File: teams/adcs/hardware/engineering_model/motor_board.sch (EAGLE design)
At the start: 63 parts

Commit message: ADCS/RW: Utilize design block in further routing progress
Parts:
- removed BRKMOD_X, BRKMOD_Y, BRKMOD_Z, CMTMOD_Y: 0_OHM_JUMPER, DubSat1 Components:0_OHM_JUMPER
- removed C16: 2.2uF, rcl:C-USC1206
- removed C17, C19: 0.1uF, rcl:C-USC0805
- removed C18, C20: 1uF, rcl:C-USC1206
- removed R25, R26, R27, R32: 3.3K, rcl:R-US_R0805
- removed R28, R29, R30: 10K, rcl:R-US_R0805
- removed R31: (no value), rcl:R-US_R0805
- removed U$12: DRV10970, DubSat1 Components:DRV10970
- added C1: 2.2uF, rcl:C-USC1206
- added C2, C4: 0.1uF, rcl:C-USC0805
- added C3, C5: 1uF, rcl:C-USC1206
- added CMTMODY: 0_OHM_JUMPER, DubSat1 Components:0_OHM_JUMPER
- added R1, R2, R3, R8: 3.3K, rcl:R-US_R0805
- added R4, R5, R6: 10K, rcl:R-US_R0805
- added R7: (no value), rcl:R-US_R0805
- added SERIAL_Z, SERIAL_Z1, SERIAL_Z2: (no value), SparkFun-Connectors:CONN_03LOCK
- added U$13: DRV10970, DubSat1 Components:DRV10970
- R12: value 3.3K -> 10K
- R15: value 10K -> (none)
- R16: value (none) -> 3.3K
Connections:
- net N$20 renamed RETRY_Z
- net N$24 renamed VCP_Z
- net N$50 renamed CPP_Z
- net N$51 renamed CPN_Z
- removed net N$13: C11.1, U$7.RETRY
- removed net N$14: C13.2, U$7.VCP
- removed net N$15: R18.2, R19.1, U$7.U_HN, U$7.V_HN, U$7.W_HN
- removed net N$16: DAA_Y.SIG, U$7.DAA
- removed net N$17: CMTMOD_Y.SIG, U$7.CMTMOD
- removed net N$18: BRKMOD_Y.SIG, U$7.BRKMOD
- removed net N$21: C12.2, U$7.CPP
- removed net N$22: C12.1, U$7.CPN
- removed net N$23: MOTOR_Y.P$1, U$7.W
- removed net N$25: MOTOR_Y.P$2, U$7.V
- removed net N$30: R11.2, R12.1, U$10.U_HN, U$10.V_HN, U$10.W_HN
- removed net N$36: DAA_X.SIG, U$10.DAA
- removed net N$38: CMTMOD_X.SIG, U$10.CMTMOD
- removed net N$39: BRKMOD_X.SIG, U$10.BRKMOD
- removed net N$40: MOTOR_Y.P$6, R22.2, U$7.W_HP
- removed net N$41: MOTOR_Y.P$7, R21.2, U$7.V_HP
- removed net N$52: MOTOR_X.P$1, U$10.W
- removed net N$53: MOTOR_X.P$2, U$10.V
- removed net N$54: MOTOR_X.P$6, R15.2, U$10.W_HP
- removed net N$55: MOTOR_X.P$7, R14.2, U$10.V_HP
- removed net N$57: MOTOR_X.P$8, R13.2, U$10.U_HP
- removed net N$58: R16.2, U$10.CS
- removed net N$59: MOTOR_X.P$3, U$10.U
- removed net N$60: MOTOR_Y.P$8, R20.2, U$7.U_HP
- removed net N$61: R23.2, U$7.CS
- removed net N$62: MOTOR_Y.P$3, U$7.U
- removed net N$69: C16.1, U$12.RETRY
- removed net N$70: C18.2, U$12.VCP
- removed net N$71: R26.2, R27.1, U$12.U_HN, U$12.V_HN, U$12.W_HN
- removed net N$72: DAA_Z.SIG, U$12.DAA
- removed net N$73: CMTMOD_Z.SIG, U$12.CMTMOD
- removed net N$74: BRKMOD_Z.SIG, U$12.BRKMOD
- removed net N$75: C17.2, U$12.CPP
- removed net N$76: C17.1, U$12.CPN
- removed net N$77: MOTOR_Z.P$1, U$12.W
- removed net N$78: MOTOR_Z.P$2, U$12.V
- removed net N$79: MOTOR_Z.P$6, R30.2, U$12.W_HP
- removed net N$80: MOTOR_Z.P$7, R29.2, U$12.V_HP
- removed net N$81: MOTOR_Z.P$8, R28.2, U$12.U_HP
- removed net N$82: R31.2, U$12.CS
- removed net N$83: MOTOR_Z.P$3, U$12.U
- removed net VM_X: C10.2, U$10.VM
- removed net VM_Y: C15.2, U$7.VM
- new net BRKMOD_X: U$7.BRKMOD
- new net BRKMOD_Y: U$13.BRKMOD
- new net BRKMOD_Z: U$10.BRKMOD
- new net CMTMOD_X: CMTMOD_X.SIG, U$7.CMTMOD
- new net CMTMOD_Y: CMTMODY.SIG, U$13.CMTMOD
- new net CMTMOD_Z: CMTMOD_Z.SIG, U$10.CMTMOD
- new net CPN_X: C2.1, U$7.CPN
- new net CPN_Y: C12.1, U$13.CPN
- new net CPP_X: C2.2, U$7.CPP
- new net CPP_Y: C12.2, U$13.CPP
- new net CS_X: R7.2, U$7.CS
- new net CS_Y: R23.2, U$13.CS
- new net CS_Z: R15.2, U$10.CS
- new net DAA_X: DAA_X.SIG, U$7.DAA
- new net DAA_Y: DAA_Y.SIG, U$13.DAA
- new net DAA_Z: DAA_Z.SIG, U$10.DAA
- new net FG: U$8.P7.4_GPIO
- new net FR: U$8.P7.3_GPIO
- new net HN_X: R2.2, R3.1, U$7.U_HN, U$7.V_HN, U$7.W_HN
- new net HN_Y: R18.2, R19.1, U$13.U_HN, U$13.V_HN, U$13.W_HN
- new net HN_Z: R10.2, R11.1, U$10.U_HN, U$10.V_HN, U$10.W_HN
- new net HP_U_X: MOTOR_X.P$8, R4.2, U$7.U_HP
- new net HP_U_Y: MOTOR_Y.P$8, R20.2, U$13.U_HP
- new net HP_U_Z: MOTOR_Z.P$8, R12.2, U$10.U_HP
- new net HP_V_X: MOTOR_X.P$7, R5.2, U$7.V_HP
- new net HP_V_Y: MOTOR_Y.P$7, R21.2, U$13.V_HP
- new net HP_V_Z: MOTOR_Z.P$7, R13.2, U$10.V_HP
- new net HP_W_X: MOTOR_X.P$6, R6.2, U$7.W_HP
- new net HP_W_Y: MOTOR_Y.P$6, R22.2, U$13.W_HP
- new net HP_W_Z: MOTOR_Z.P$6, R14.2, U$10.W_HP
- new net M_Z_RX: SERIAL_Z.2, SERIAL_Z1.2, SERIAL_Z2.2, U$8.P2.6_GPIO/PWM
- new net M_Z_TX: SERIAL_Z.1, SERIAL_Z1.1, SERIAL_Z2.1, U$8.P2.5_GPIO
- new net PWM: U$8.P1.7_GPIO/PWM
- new net RD: U$8.P4.0_GPIO
- new net RETRY_X: C1.1, U$7.RETRY
- new net RETRY_Z_Y: C11.1, U$13.RETRY
- new net U_X: MOTOR_X.P$3, U$7.U
- new net U_Y: MOTOR_Y.P$3, U$13.U
- new net U_Z: MOTOR_Z.P$3, U$10.U
- new net V1_Z: MOTOR_Z.P$2, U$10.V
- new net VCP_X: C3.2, U$7.VCP
- new net VCP_Y: C13.2, U$13.VCP
- new net VM: C15.2, C5.2, U$13.VM, U$7.VM
- new net V_X: MOTOR_X.P$2, U$7.V
- new net V_Y: MOTOR_Y.P$2, U$13.V
- new net W_X: MOTOR_X.P$1, U$7.W
- new net W_Y: MOTOR_Y.P$1, U$13.W
- new net W_Z: MOTOR_Z.P$1, U$10.W
- net FG_X: now also R8.2, U$7.FG; no longer R17.2, U$10.FG
- net FG_Y: now also U$13.FG; no longer U$7.FG
- net FG_Z: now also R16.2, U$10.FG; no longer R32.2, U$12.FG, U$8.P7.4_GPIO
- net FR_X: now also U$7.FR; no longer U$10.FR
- net FR_Y: now also U$13.FR; no longer U$7.FR
- net FR_Z: now also U$10.FR; no longer U$12.FR, U$8.P7.3_GPIO
- net GND: now also C1.2, C3.1, C4.1, C5.1, CMTMODY.GND, R10.1, R15.1, R2.1, R7.1, SERIAL_Z.3, SERIAL_Z1.3, SERIAL_Z2.3, U$13.GND; no longer BRKMOD_X.GND, BRKMOD_Y.GND, BRKMOD_Z.GND, C16.2, C18.1, C19.1, C20.1, CMTMOD_Y.GND, R11.1, R16.1, R26.1, R31.1, U$12.GND
- net PWM_X: now also U$7.PWM; no longer U$10.PWM
- net PWM_Y: now also U$13.PWM; no longer U$7.PWM
- net PWM_Z: now also U$10.PWM; no longer U$12.PWM, U$8.P1.7_GPIO/PWM
- net RD_X: now also R1.1, U$7.RD; no longer R9.1, U$10.RD
- net RD_Y: now also R17.1, U$13.RD; no longer R10.1, U$7.RD
- net RD_Z: now also R9.1, U$10.RD; no longer R25.1, U$12.RD, U$8.P4.0_GPIO
- net VINT_X: now also C4.2, R1.2, R3.2, R4.1, R5.1, R6.1, R8.1, U$7.VINT; no longer BRKMOD_X.VCC, C9.2, R12.2, R13.1, R14.1, R15.1, R17.1, R9.2, U$10.VINT
- net VINT_Y: now also CMTMODY.VCC, R17.2, U$13.VINT; no longer BRKMOD_Y.VCC, CMTMOD_Y.VCC, R10.2, U$7.VINT
- net VINT_Z: now also C9.2, R11.2, R12.1, R13.1, R14.1, R16.1, R9.2, U$10.VINT; no longer BRKMOD_Z.VCC, C19.2, R25.2, R27.2, R28.1, R29.1, R30.1, R32.1, U$12.VINT
- net VM_Z: now also C10.2, U$10.VM; no longer C20.2, U$12.VM
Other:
- moved on the sheet: C10, C11, C12, C13, C14, C15, C6, C7, C8, C9, CMTMOD_X, CMTMOD_Z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

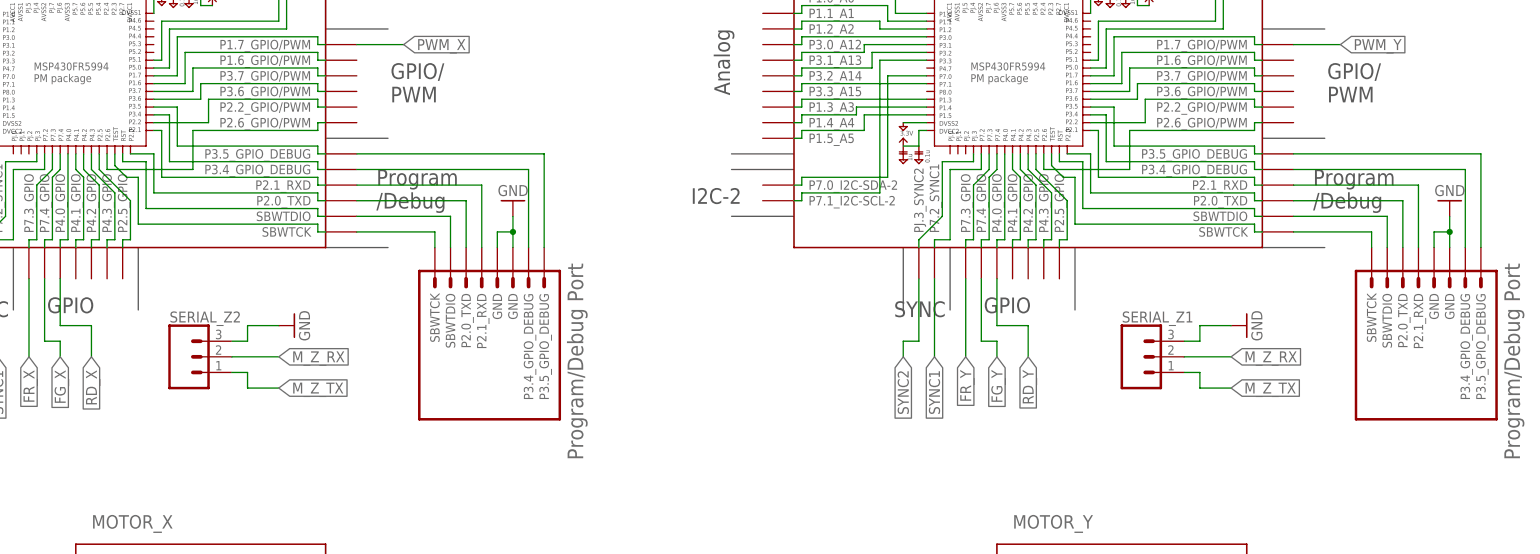
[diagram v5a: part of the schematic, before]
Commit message: ADCS/RW: Further routing
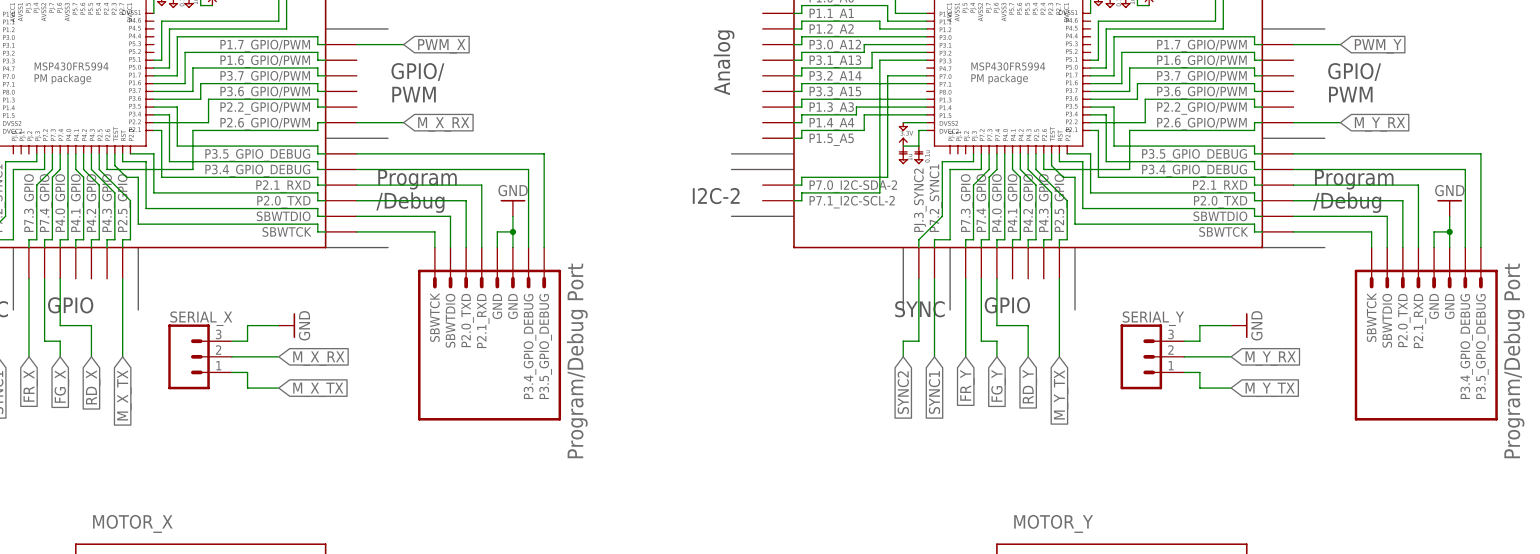
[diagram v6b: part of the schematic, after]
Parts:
- renumbered SERIAL_Z1 to SERIAL_Y, SERIAL_Z2 to SERIAL_X
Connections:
- new net M_X_RX: SERIAL_X.2, U$3.P2.6_GPIO/PWM
- new net M_X_TX: SERIAL_X.1, U$3.P2.5_GPIO
- new net M_Y_RX: SERIAL_Y.2, U$5.P2.6_GPIO/PWM
- new net M_Y_TX: SERIAL_Y.1, U$5.P2.5_GPIO
- net M_Z_RX: no longer SERIAL_X.2, SERIAL_Y.2
- net M_Z_TX: no longer SERIAL_X.1, SERIAL_Y.1
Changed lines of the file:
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@@
 <part name="GND32" library="supply1" library_urn="urn:adsk.eagle:library:371" deviceset="GND" device=""/>
 <part name="GND33" library="supply1" library_urn="urn:adsk.eagle:library:371" deviceset="GND" device=""/>
-<part name="SERIAL_Z1" library="SparkFun-Connectors" deviceset="CONN_03" device="LOCK"/>
+<part name="SERIAL_Y" library="SparkFun-Connectors" deviceset="CONN_03" device="LOCK"/>
 <part name="GND36" library="supply1" library_urn="urn:adsk.eagle:library:371" deviceset="GND" device=""/>
-<part name="SERIAL_Z2" library="SparkFun-Connectors" deviceset="CONN_03" device="LOCK"/>
+<part name="SERIAL_X" library="SparkFun-Connectors" deviceset="CONN_03" device="LOCK"/>
 <part name="GND37" library="supply1" library_urn="urn:adsk.eagle:library:371" deviceset="GND" device=""/>
 </parts>
@@
 <instance part="GND32" gate="1" x="289.56" y="-307.34"/>
 <instance part="GND33" gate="1" x="307.34" y="-289.56"/>
-<instance part="SERIAL_Z1" gate="J$1" x="172.72" y="-129.54"/>
+<instance part="SERIAL_Y" gate="J$1" x="172.72" y="-129.54"/>
 <instance part="GND36" gate="1" x="190.5" y="-124.46" rot="R90"/>
-<instance part="SERIAL_Z2" gate="J$1" x="17.78" y="-129.54"/>
+<instance part="SERIAL_X" gate="J$1" x="17.78" y="-129.54"/>
 <instance part="GND37" gate="1" x="35.56" y="-124.46" rot="R90"/>
 </instances>
@@
 </segment>
 <segment>
-<pinref part="SERIAL_Z1" gate="J$1" pin="3"/>
+<pinref part="SERIAL_Y" gate="J$1" pin="3"/>
 <wire x1="180.34" y1="-127" x2="182.88" y2="-127" width="0.1524" layer="91"/>
 <wire x1="182.88" y1="-127" x2="182.88" y2="-124.46" width="0.1524" layer="91"/>
@@
 </segment>
 <segment>
-<pinref part="SERIAL_Z2" gate="J$1" pin="3"/>
+<pinref part="SERIAL_X" gate="J$1" pin="3"/>
 <wire x1="25.4" y1="-127" x2="27.94" y2="-127" width="0.1524" layer="91"/>
 <wire x1="27.94" y1="-127" x2="27.94" y2="-124.46" width="0.1524" layer="91"/>
@@
 <label x="345.44" y="-137.16" size="1.778" layer="95" xref="yes"/>
 </segment>
-<segment>
-<pinref part="SERIAL_Z1" gate="J$1" pin="1"/>
-<wire x1="180.34" y1="-132.08" x2="182.88" y2="-132.08" width="0.1524" layer="91"/>
-<wire x1="182.88" y1="-132.08" x2="182.88" y2="-134.62" width="0.1524" layer="91"/>
-<wire x1="182.88" y1="-134.62" x2="187.96" y2="-134.62" width="0.1524" layer="91"/>
-<label x="187.96" y="-134.62" size="1.778" layer="95" xref="yes"/>
-</segment>
-<segment>
-<pinref part="SERIAL_Z2" gate="J$1" pin="1"/>
-<wire x1="25.4" y1="-132.08" x2="27.94" y2="-132.08" width="0.1524" layer="91"/>
-<wire x1="27.94" y1="-132.08" x2="27.94" y2="-134.62" width="0.1524" layer="91"/>
-<wire x1="27.94" y1="-134.62" x2="33.02" y2="-134.62" width="0.1524" layer="91"/>
-<label x="33.02" y="-134.62" size="1.778" layer="95" xref="yes"/>
-</segment>
 </net>
 <net name="M_Z_RX" class="0">
@@
 <wire x1="337.82" y1="-132.08" x2="345.44" y2="-132.08" width="0.1524" layer="91"/>
 <label x="345.44" y="-132.08" size="1.778" layer="95" xref="yes"/>
-</segment>
-<segment>
-<pinref part="SERIAL_Z1" gate="J$1" pin="2"/>
-<wire x1="180.34" y1="-129.54" x2="187.96" y2="-129.54" width="0.1524" layer="91"/>
-<label x="187.96" y="-129.54" size="1.778" layer="95" xref="yes"/>
-</segment>
-<segment>
-<pinref part="SERIAL_Z2" gate="J$1" pin="2"/>
-<wire x1="25.4" y1="-129.54" x2="33.02" y2="-129.54" width="0.1524" layer="91"/>
-<label x="33.02" y="-129.54" size="1.778" layer="95" xref="yes"/>
 </segment>
 </net>
@@
 </segment>
 </net>
+<net name="M_X_RX" class="0">
+<segment>
+<pinref part="SERIAL_X" gate="J$1" pin="2"/>
+<wire x1="25.4" y1="-129.54" x2="33.02" y2="-129.54" width="0.1524" layer="91"/>
+<label x="33.02" y="-129.54" size="1.778" layer="95" xref="yes"/>
+</segment>
+<segment>
+<pinref part="U$3" gate="G$1" pin="P2.6_GPIO/PWM"/>
+<wire x1="45.72" y1="-91.44" x2="53.34" y2="-91.44" width="0.1524" layer="91"/>
+<label x="53.34" y="-91.44" size="1.778" layer="95" xref="yes"/>
+</segment>
+</net>
+<net name="M_X_TX" class="0">
+<segment>
+<pinref part="SERIAL_X" gate="J$1" pin="1"/>
+<wire x1="25.4" y1="-132.08" x2="27.94" y2="-132.08" width="0.1524" layer="91"/>
+<wire x1="27.94" y1="-132.08" x2="27.94" y2="-134.62" width="0.1524" layer="91"/>
+<wire x1="27.94" y1="-134.62" x2="33.02" y2="-134.62" width="0.1524" layer="91"/>
+<label x="33.02" y="-134.62" size="1.778" layer="95" xref="yes"/>
+</segment>
+<segment>
+<pinref part="U$3" gate="G$1" pin="P2.5_GPIO"/>
+<wire x1="7.62" y1="-116.84" x2="7.62" y2="-129.54" width="0.1524" layer="91"/>
+<label x="7.62" y="-129.54" size="1.778" layer="95" rot="R270" xref="yes"/>
+</segment>
+</net>
+<net name="M_Y_RX" class="0">
+<segment>
+<pinref part="SERIAL_Y" gate="J$1" pin="2"/>
+<wire x1="180.34" y1="-129.54" x2="187.96" y2="-129.54" width="0.1524" layer="91"/>
+<label x="187.96" y="-129.54" size="1.778" layer="95" xref="yes"/>
+</segment>
+<segment>
+<pinref part="U$5" gate="G$1" pin="P2.6_GPIO/PWM"/>
+<wire x1="198.12" y1="-91.44" x2="205.74" y2="-91.44" width="0.1524" layer="91"/>
+<label x="205.74" y="-91.44" size="1.778" layer="95" xref="yes"/>
+</segment>
+</net>
+<net name="M_Y_TX" class="0">
+<segment>
+<pinref part="SERIAL_Y" gate="J$1" pin="1"/>
+<wire x1="180.34" y1="-132.08" x2="182.88" y2="-132.08" width="0.1524" layer="91"/>
+<wire x1="182.88" y1="-132.08" x2="182.88" y2="-134.62" width="0.1524" layer="91"/>
+<wire x1="182.88" y1="-134.62" x2="187.96" y2="-134.62" width="0.1524" layer="91"/>
+<label x="187.96" y="-134.62" size="1.778" layer="95" xref="yes"/>
+</segment>
+<segment>
+<pinref part="U$5" gate="G$1" pin="P2.5_GPIO"/>
+<wire x1="160.02" y1="-116.84" x2="160.02" y2="-129.54" width="0.1524" layer="91"/>
+<label x="160.02" y="-129.54" size="1.778" layer="95" rot="R270" xref="yes"/>
+</segment>
+</net>
